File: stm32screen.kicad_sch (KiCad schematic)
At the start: 33 parts, among them J1 SWD, J2 GC9A01, J3 OIL, J4 PRESS, J5 POWER IN, SW1 NRST, SW2 USER, U1 TS1117BCW-3.3, U2 STM32F407VETx

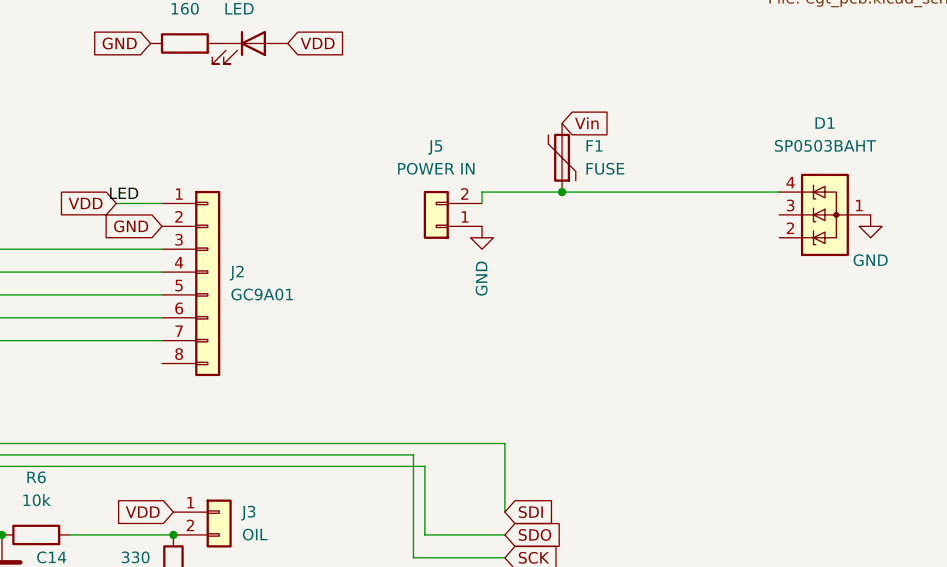
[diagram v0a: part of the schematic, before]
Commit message: Changed display conn symbol, added NC flags. Corrected silkscreen labels
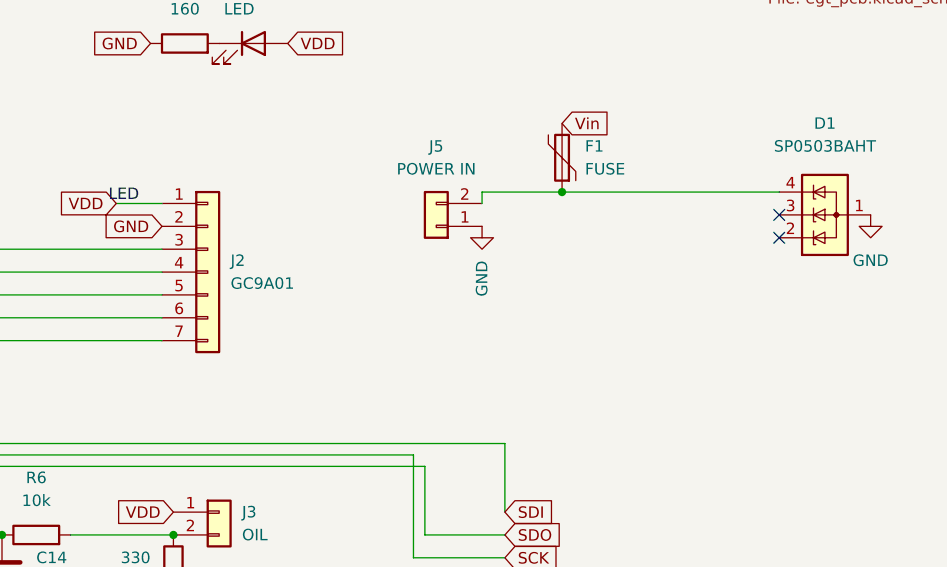
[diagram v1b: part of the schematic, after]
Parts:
- J2: symbol Connector_Generic:Conn_01x08 -> Connector_Generic:Conn_01x07
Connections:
- no-connect marks 0 -> 2
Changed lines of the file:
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@@
 		(color 0 0 0 0)
+	)
+	(no_connect
+		(at 200.66 91.44)
+	)
+	(no_connect
+		(at 200.66 93.98)
 	)
 	(wire
@@
 	)
 	(symbol
-		(lib_id "Connector_Generic:Conn_01x08")
+		(lib_id "Connector_Generic:Conn_01x07")
 		(at 137.16 97.79 0)
 		(unit 1)
@@
 		(fields_autoplaced yes)
 		(property "Reference" "J2"
-			(at 139.7 97.7899 0)
+			(at 139.7 96.5199 0)
 			(effects
 				(font
@@
 		)
 		(property "Value" "GC9A01"
-			(at 139.7 100.3299 0)
+			(at 139.7 99.0599 0)
 			(effects
 				(font
@@
 			)
 		)
-		(property "Description" ""
+		(property "Description" "Generic connector, single row, 01x07, script generated (kicad-library-utils/schlib/autogen/connector/)"
 			(at 137.16 97.79 0)
 			(effects
@@
 					(size 1.27 1.27)
 				)
+				(hide yes)
 			)
 		)
@@
 		(pin "7"
 		)
-		(pin "8"
-		)
 		(instances

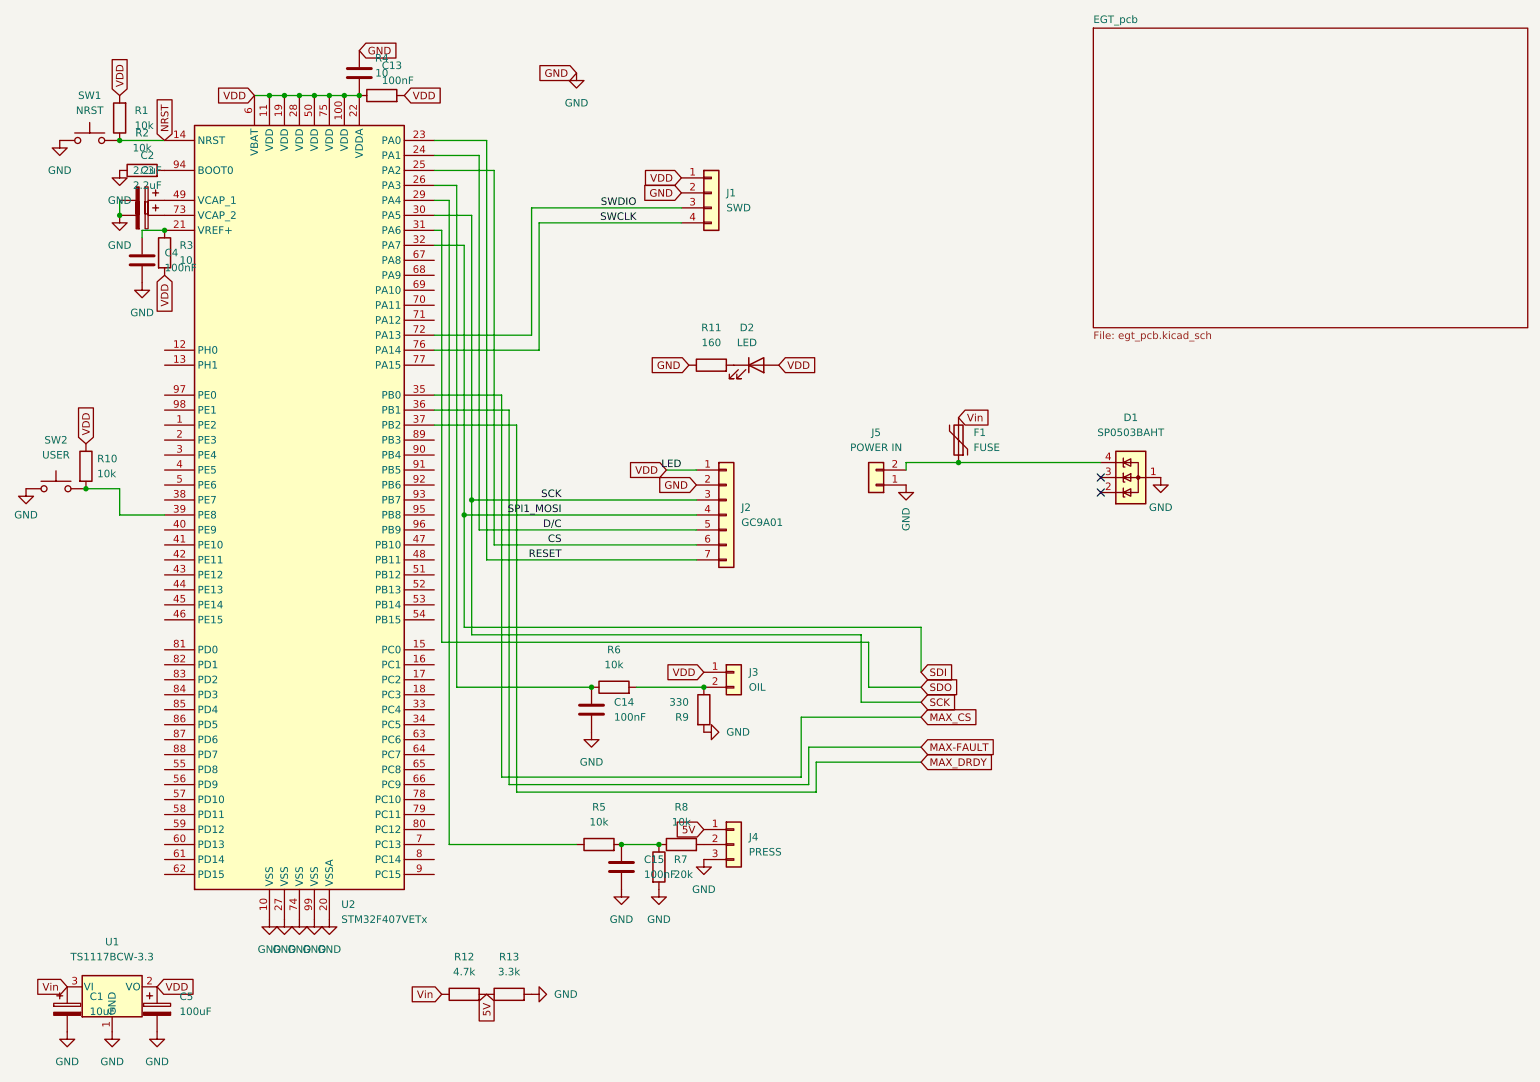
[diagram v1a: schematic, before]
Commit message: Switched from SP0503BAHT to SMBJ24A for a TVS Diode, since we're using 12v supply now instead of 5v
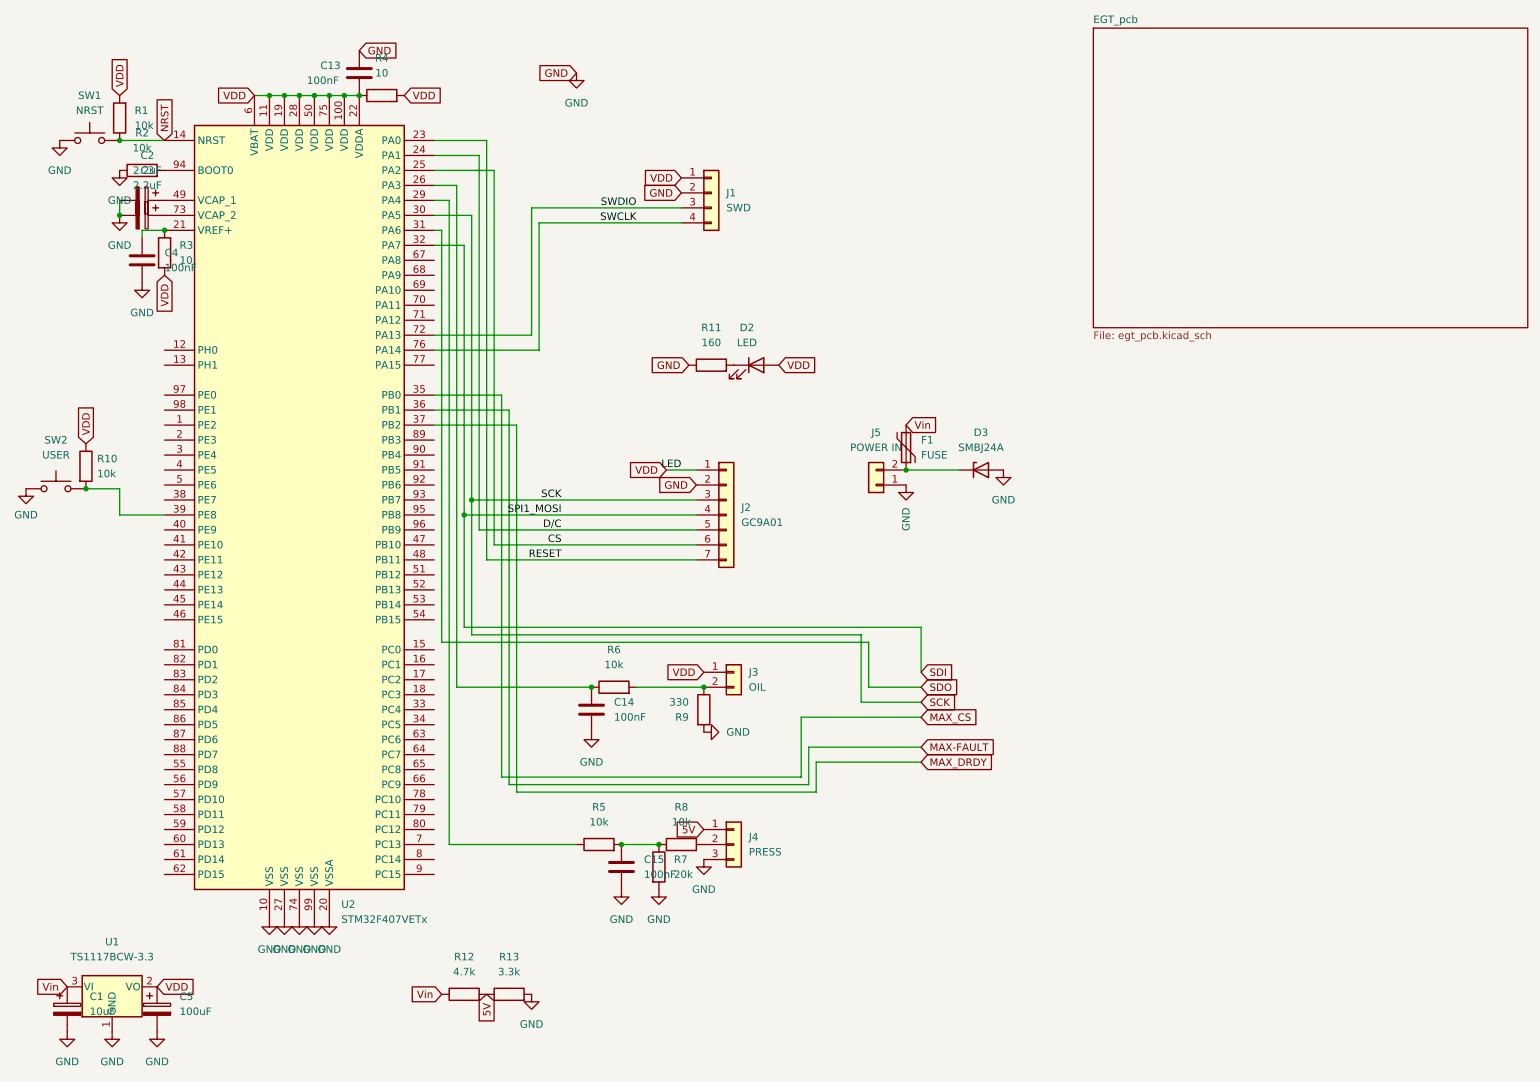
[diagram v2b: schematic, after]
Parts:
- removed D1: SP0503BAHT, Package_TO_SOT_SMD:SOT-143, symbol Power_Protection:SP0503BAHT
- added D3: SMBJ24A, Diode_SMD:D_SMB_Handsoldering, symbol Diode:Z2SMBxxx
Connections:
- net GND: now also D3.2 (A)
- net at F1.1, J5.2 (Pin_2): now also D3.1 (K)
- no-connect marks 2 -> 0
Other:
- moved on the sheet: F1
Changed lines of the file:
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@@
 	)
 	(junction
+		(at 167.64 90.17)
+		(diameter 0)
+		(color 0 0 0 0)
+	)
+	(junction
 		(at 64.77 26.67)
 		(diameter 0)
@@
 	)
 	(junction
-		(at 176.53 88.9)
-		(diameter 0)
-		(color 0 0 0 0)
-	)
-	(junction
 		(at 92.71 97.79)
 		(diameter 0)
@@
 		(color 0 0 0 0)
 	)
-	(no_connect
-		(at 200.66 91.44)
-	)
-	(no_connect
-		(at 200.66 93.98)
-	)
 	(wire
 		(pts
@@
 	(wire
 		(pts
-			(xy 105.41 48.26) (xy 129.54 48.26)
+			(xy 167.64 90.17) (xy 176.53 90.17)
 		)
 		(stroke
@@
 	(wire
 		(pts
-			(xy 151.13 137.16) (xy 170.18 137.16)
+			(xy 105.41 48.26) (xy 129.54 48.26)
 		)
 		(stroke
@@
 	(wire
 		(pts
-			(xy 38.1 49.53) (xy 41.91 49.53)
+			(xy 151.13 137.16) (xy 170.18 137.16)
 		)
 		(stroke
@@
 	(wire
 		(pts
-			(xy 92.71 97.79) (xy 92.71 116.84)
+			(xy 38.1 49.53) (xy 41.91 49.53)
 		)
 		(stroke
@@
 	(wire
 		(pts
-			(xy 34.29 34.29) (xy 41.91 34.29)
+			(xy 92.71 97.79) (xy 92.71 116.84)
 		)
 		(stroke
@@
 	(wire
 		(pts
-			(xy 100.33 143.51) (xy 151.13 143.51)
+			(xy 34.29 34.29) (xy 41.91 34.29)
 		)
 		(stroke
@@
 	(wire
 		(pts
-			(xy 90.17 153.67) (xy 111.76 153.67)
+			(xy 100.33 143.51) (xy 151.13 143.51)
 		)
 		(stroke
@@
 	(wire
 		(pts
-			(xy 176.53 88.9) (xy 167.64 88.9)
+			(xy 90.17 153.67) (xy 111.76 153.67)
 		)
 		(stroke
@@
 	(wire
 		(pts
-			(xy 176.53 88.9) (xy 200.66 88.9)
-		)
-		(stroke
-			(width 0)
-			(type default)
-		)
-	)
-	(wire
-		(pts
 			(xy 100.33 80.01) (xy 100.33 143.51)
 		)
@@
 	(wire
 		(pts
-			(xy 167.64 88.9) (xy 167.64 90.17)
-		)
-		(stroke
-			(width 0)
-			(type default)
-		)
-	)
-	(wire
-		(pts
 			(xy 101.6 82.55) (xy 87.63 82.55)
 		)
@@
 	(global_label "Vin"
 		(shape input)
-		(at 176.53 81.28 0)
+		(at 167.64 82.55 0)
 		(fields_autoplaced yes)
 		(effects
@@
 		)
 		(property "Intersheetrefs" "${INTERSHEET_REFS}"
-			(at 176.53 81.28 0)
+			(at 167.64 82.55 0)
 			(effects
 				(font
@@
 		)
 		(property "Välilehtien väliset viitteet" "${INTERSHEET_REFS}"
-			(at 181.7855 81.2006 0)
+			(at 172.8955 82.4706 0)
 			(effects
 				(font
@@
 		(lib_name "GND_1")
 		(lib_id "power:GND")
-		(at 104.14 179.07 90)
+		(at 104.14 179.07 0)
 		(unit 1)
 		(exclude_from_sim no)
@@
 		(fields_autoplaced yes)
 		(property "Reference" "#PWR019"
-			(at 110.49 179.07 0)
+			(at 104.14 185.42 0)
 			(effects
 				(font
@@
 		)
 		(property "Value" "GND"
-			(at 107.95 179.0699 90)
+			(at 104.14 184.15 0)
 			(effects
 				(font
 					(size 1.27 1.27)
 				)
-				(justify right)
 			)
 		)
@@
 		(on_board yes)
 		(dnp no)
-		(fields_autoplaced yes)
 		(property "Reference" "C13"
-			(at 78.74 21.5899 0)
+			(at 68.326 21.59 0)
 			(effects
 				(font
@@
 		)
 		(property "Value" "100nF"
-			(at 78.74 24.1299 0)
+			(at 66.04 24.13 0)
 			(effects
 				(font
@@
 	(symbol
 		(lib_id "power:GND")
-		(at 210.82 91.44 0)
+		(at 184.15 90.17 0)
+		(mirror y)
 		(unit 1)
 		(exclude_from_sim no)
@@
 		(on_board yes)
 		(dnp no)
-		(fields_autoplaced yes)
 		(property "Reference" "#PWR0101"
-			(at 210.82 97.79 0)
+			(at 184.15 96.52 0)
 			(effects
 				(font
@@
 		)
 		(property "Value" "GND"
-			(at 210.82 96.52 0)
+			(at 184.15 95.25 0)
 			(effects
 				(font
@@
 		)
 		(property "Footprint" ""
-			(at 210.82 91.44 0)
+			(at 184.15 90.17 0)
 			(effects
 				(font
@@
 		)
 		(property "Datasheet" ""
-			(at 210.82 91.44 0)
+			(at 184.15 90.17 0)
 			(effects
 				(font
@@
 		)
 		(property "Description" ""
-			(at 210.82 91.44 0)
+			(at 184.15 90.17 0)
 			(effects
 				(font
@@
 	)
 	(symbol
-		(lib_id "Power_Protection:SP0503BAHT")
-		(at 205.74 91.44 90)
-		(unit 1)
-		(exclude_from_sim no)
-		(in_bom yes)
-		(on_board yes)
-		(dnp no)
-		(fields_autoplaced yes)
-		(property "Reference" "D1"
-			(at 205.74 81.28 90)
-			(effects
-				(font
-					(size 1.27 1.27)
-				)
-			)
-		)
-		(property "Value" "SP0503BAHT"
-			(at 205.74 83.82 90)
-			(effects
-				(font
-					(size 1.27 1.27)
-				)
-			)
-		)
-		(property "Footprint" "Package_TO_SOT_SMD:SOT-143"
-			(at 207.01 85.725 0)
-			(effects
-				(font
-					(size 1.27 1.27)
-				)
-				(justify left)
-				(hide yes)
-			)
-		)
-		(property "Datasheet" "http://www.littelfuse.com/~/media/files/littelfuse/technical%20resources/documents/data%20sheets/sp05xxba.pdf"
-			(at 202.565 88.265 0)
-			(effects
-				(font
-					(size 1.27 1.27)
-				)
-				(hide yes)
-			)
-		)
-		(property "Description" ""
-			(at 205.74 91.44 0)
-			(effects
-				(font
-					(size 1.27 1.27)
-				)
-			)
-		)
-		(pin "1"
-		)
-		(pin "2"
-		)
-		(pin "3"
-		)
-		(pin "4"
-		)
-		(instances
-			(project ""
-				(path "/dd9634c9-b7ae-401f-800b-241ca4b8e751"
-					(reference "D1")
-					(unit 1)
-				)
-			)
-		)
-	)
-	(symbol
 		(lib_id "power:GND")
 		(at 18.415 93.345 0)
@@
 	(symbol
 		(lib_id "Device:Polyfuse")
-		(at 176.53 85.09 180)
+		(at 167.64 86.36 180)
 		(unit 1)
 		(exclude_from_sim no)
@@
 		(fields_autoplaced yes)
 		(property "Reference" "F1"
-			(at 179.07 83.8199 0)
+			(at 170.18 85.0899 0)
 			(effects
 				(font
@@
 		)
 		(property "Value" "FUSE"
-			(at 179.07 86.3599 0)
+			(at 170.18 87.6299 0)
 			(effects
 				(font
@@
 		)
 		(property "Footprint" "Fuse:Fuse_0805_2012Metric_Pad1.15x1.40mm_HandSolder"
-			(at 175.26 80.01 0)
+			(at 166.37 81.28 0)
 			(effects
 				(font
@@
 		)
 		(property "Datasheet" "~"
-			(at 176.53 85.09 0)
+			(at 167.64 86.36 0)
 			(effects
 				(font
@@
 		)
 		(property "Description" ""
-			(at 176.53 85.09 0)
+			(at 167.64 86.36 0)
 			(effects
 				(font
@@
 					(unit 1)
 				)
+			)
+		)
+	)
+	(symbol
+		(lib_id "Diode:Z2SMBxxx")
+		(at 180.34 90.17 0)
+		(unit 1)
+		(exclude_from_sim no)
+		(in_bom yes)
+		(on_board yes)
+		(dnp no)
+		(fields_autoplaced yes)
+		(property "Reference" "D3"
+			(at 180.34 83.82 0)
+			(effects
+				(font
+					(size 1.27 1.27)
+				)
+			)
+		)
+		(property "Value" "SMBJ24A"
+			(at 180.34 86.36 0)
+			(effects
+				(font
+					(size 1.27 1.27)
+				)
+			)
+		)
+		(property "Footprint" "Diode_SMD:D_SMB_Handsoldering"
+			(at 180.34 94.615 0)
+			(effects
+				(font
+					(size 1.27 1.27)
+				)
+				(hide yes)
+			)
+		)
+		(property "Datasheet" "https://diotec.com/tl_files/diotec/files/pdf/datasheets/z2smb1.pdf"
+			(at 180.34 90.17 0)
+			(effects
+				(font
+					(size 1.27 1.27)
+				)
+				(hide yes)
+			)
+		)
+		(property "Description" "2000mW Zener Diode, SMB(DO-214AA)"
+			(at 180.34 90.17 0)
+			(effects
+				(font
+					(size 1.27 1.27)
+				)
+				(hide yes)
+			)
+		)
+		(pin "1"
+		)
+		(pin "2"
+		)
+		(instances
+			(project ""
+				(path "/dd9634c9-b7ae-401f-800b-241ca4b8e751"
+					(reference "D3")
+					(unit 1)
+				)
